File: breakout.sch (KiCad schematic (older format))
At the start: 36 parts, among them CON1 SD_Card, CON2 USB-MICRO-AB, P2 CONN_01X40, P3 CONN_01X40, P4 CONN_01X40, P5 A-DF-09-A/KG-T4S, Q1 SIA461DJ-T1-GE3, Q2 IRLML2402TRPBF, SW1 SW_PUSH

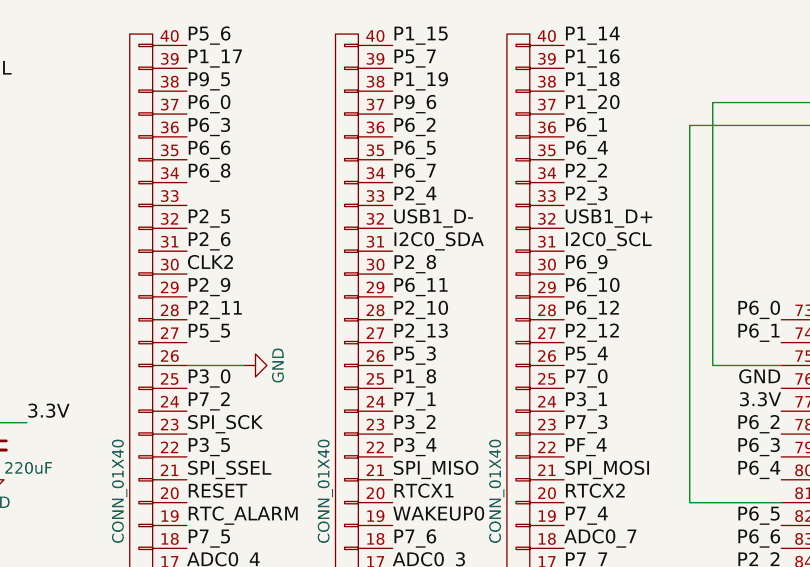
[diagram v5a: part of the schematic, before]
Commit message: P1_1 & P1_2 to header; trace move to aid GND plane
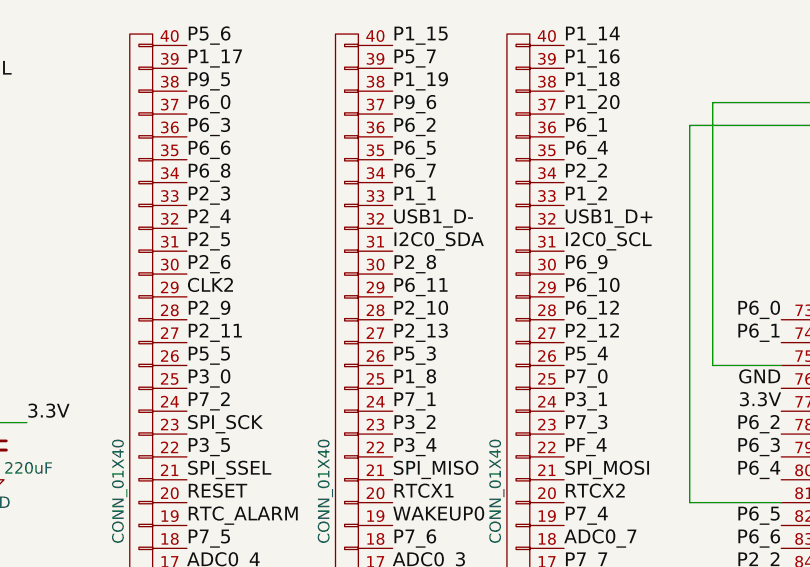
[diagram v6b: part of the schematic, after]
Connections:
- net CLK2: now also P2.29 (P29); no longer P2.30 (P30)
- net GND: no longer P2.26 (P26)
- net P1_1: now also P3.33 (P33)
- net P1_2: now also P4.33 (P33)
- net P2_11: now also P2.27 (P27); no longer P2.28 (P28)
- net P2_3: now also P2.33 (P33); no longer P4.33 (P33)
- net P2_4: now also P2.32 (P32); no longer P3.33 (P33)
- net P2_5: now also P2.31 (P31); no longer P2.32 (P32)
- net P2_6: now also P2.30 (P30); no longer P2.31 (P31)
- net P2_9: now also P2.28 (P28); no longer P2.29 (P29)
- net P5_5: now also P2.26 (P26); no longer P2.27 (P27)
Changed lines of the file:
@@
 Text Label 4500 1600 0    60   ~ 0
 I2C0_SCL
-Text Label 2850 1500 0    60   ~ 0
+Text Label 2850 1600 0    60   ~ 0
 P2_5
 Text Label 3750 1500 0    60   ~ 0
@@
 Text Label 4500 1500 0    60   ~ 0
 USB1_D+
-Text Label 3750 1400 0    60   ~ 0
+Text Label 2850 1500 0    60   ~ 0
 P2_4
 Text Label 2850 1300 0    60   ~ 0
@@
 Text Label 4500 2000 0    60   ~ 0
 P2_12
-Text Label 2850 1900 0    60   ~ 0
+Text Label 2850 2000 0    60   ~ 0
 P2_11
 Text Label 3750 1900 0    60   ~ 0
@@
 Text Label 4500 1900 0    60   ~ 0
 P6_12
-Text Label 2850 1800 0    60   ~ 0
+Text Label 2850 1900 0    60   ~ 0
 P2_9
 Text Label 3750 1800 0    60   ~ 0
@@
 Text Label 4500 1800 0    60   ~ 0
 P6_10
-Text Label 2850 1700 0    60   ~ 0
+Text Label 2850 1800 0    60   ~ 0
 CLK2
 Text Label 3750 1700 0    60   ~ 0
@@
 Text Label 4500 1700 0    60   ~ 0
 P6_9
-Text Label 2850 1600 0    60   ~ 0
+Text Label 2850 1700 0    60   ~ 0
 P2_6
-Text Label 4500 1400 0    60   ~ 0
+Text Label 2850 1400 0    60   ~ 0
 P2_3
-Text Label 2850 2000 0    60   ~ 0
+Text Label 2850 2100 0    60   ~ 0
 P5_5
 Text Label 4500 2100 0    60   ~ 0
@@
 	5050 2700 5450 2700
 $Comp
-L GND #PWR018
-U 1 1 566387B9
-P 3100 2100
-F 0 "#PWR018" H 3100 1850 50  0001 C CNN
-F 1 "GND" H 3100 1950 50  0000 C CNN
-F 2 "" H 3100 2100 60  0000 C CNN
-F 3 "" H 3100 2100 60  0000 C CNN
-	1    3100 2100
-	0    -1   -1   0
-$EndComp
-Wire Wire Line
-	2850 2100 3100 2100
-$Comp
 L SIA461DJ-T1-GE3 Q1
 U 1 1 5664957E
@@
 $EndComp
 $Comp
-L GND #PWR019
+L GND #PWR018
 U 1 1 56644987
 P 800 4900
-F 0 "#PWR019" H 800 4650 50  0001 C CNN
+F 0 "#PWR018" H 800 4650 50  0001 C CNN
 F 1 "GND" H 800 4750 50  0000 C CNN
 F 2 "" H 800 4900 60  0000 C CNN
@@
 3.3V
 $Comp
-L GND #PWR020
+L GND #PWR019
 U 1 1 566486A9
 P 7800 6800
-F 0 "#PWR020" H 7800 6550 50  0001 C CNN
+F 0 "#PWR019" H 7800 6550 50  0001 C CNN
 F 1 "GND" H 7800 6650 50  0000 C CNN
 F 2 "" H 7800 6800 60  0000 C CNN
@@
 	7800 6800 7450 6800
 $Comp
-L GND #PWR021
+L GND #PWR020
 U 1 1 5664879C
 P 7800 7150
-F 0 "#PWR021" H 7800 6900 50  0001 C CNN
+F 0 "#PWR020" H 7800 6900 50  0001 C CNN
 F 1 "GND" H 7800 7000 50  0000 C CNN
 F 2 "" H 7800 7150 60  0000 C CNN
@@
 Text Label 2850 2700 0    60   ~ 0
 RESET
+Text Label 4500 1400 0    60   ~ 0
+P1_2
+Text Label 3750 1400 0    60   ~ 0
+P1_1
 $EndSCHEMATC

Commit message: RAIL, UNREG, 5V
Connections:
- net 5V: now also P4.1 (P1)
- net GND: now also P2.1 (P1), P3.1 (P1), P4.2 (P2)
- net RAIL: now also P4.4 (P4)
- net UNREG: now reaches D2.1 (A), POWER1.2 (P2)
- net UNREG: now also P4.3 (P3)
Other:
- moved on the sheet: D2
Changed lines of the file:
@@
 Text Label 1600 750  0    60   ~ 0
 GND
-Text Label 1900 850  0    60   ~ 0
+Text Label 2050 850  0    60   ~ 0
 RAIL
 Text Label 5450 5500 2    60   ~ 0
@@
 L D_Schottky D2
 U 1 1 564CF908
-P 1750 850
-F 0 "D2" H 1850 800 50  0000 C CNN
-F 1 "B340" H 1700 950 50  0000 C CNN
-F 2 "Diodes_SMD:Diode-SMC_Standard" H 1750 850 60  0001 C CNN
-F 3 "" H 1750 850 60  0000 C CNN
-	1    1750 850
+P 1900 850
+F 0 "D2" H 2000 800 50  0000 C CNN
+F 1 "B340" H 1850 950 50  0000 C CNN
+F 2 "Diodes_SMD:Diode-SMC_Standard" H 1900 850 60  0001 C CNN
+F 3 "" H 1900 850 60  0000 C CNN
+	1    1900 850
 	1    0    0    1
 $EndComp
@@
 	900  6350 1000 6450
 Wire Bus Line
-	2600 6350 850  6350
+	850  6350 2600 6350
 Connection ~ 2350 5800
 Text Label 2850 2700 0    60   ~ 0
@@
 Text Label 3750 1400 0    60   ~ 0
 P1_1
+Text Label 4500 4600 0    60   ~ 0
+5V
+Text Label 4500 4300 0    60   ~ 0
+RAIL
+Text Label 1500 1150 2    60   ~ 0
+UNREG
+Wire Wire Line
+	1600 850  1600 1150
+Wire Wire Line
+	1750 850  1600 850
+Wire Wire Line
+	1600 1150 1500 1150
+Text Label 4500 4400 0    60   ~ 0
+UNREG
+Text Label 4500 4500 0    60   ~ 0
+GND
+Text Label 3750 4600 0    60   ~ 0
+GND
+Text Label 2850 4600 0    60   ~ 0
+GND
 $EndSCHEMATC

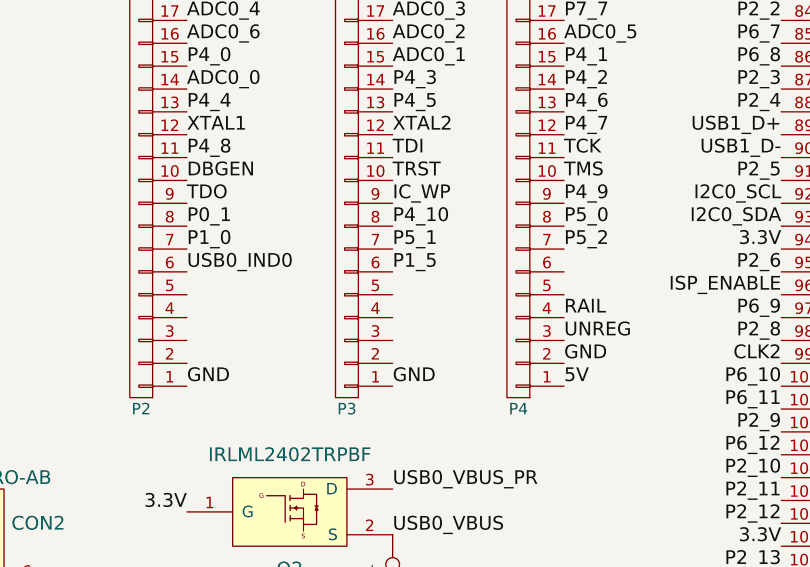
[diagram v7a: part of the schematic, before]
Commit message: added P1_3 and fixed annular ring of vias
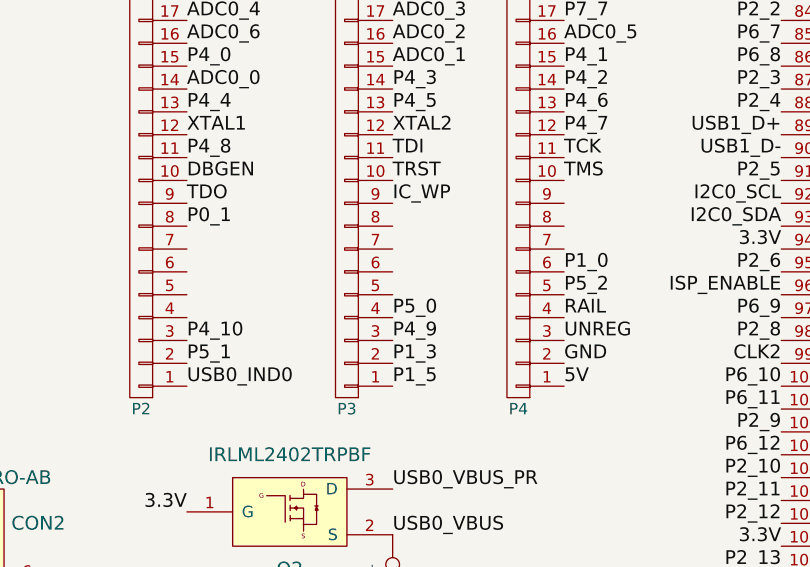
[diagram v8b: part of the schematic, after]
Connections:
- net GND: no longer P2.1 (P1), P3.1 (P1)
- net P1_0: now also P4.6 (P6); no longer P2.7 (P7)
- net P1_3: now also P3.2 (P2)
- net P1_5: now also P3.1 (P1); no longer P3.6 (P6)
- net P4_10: now also P2.3 (P3); no longer P3.8 (P8)
- net P4_9: now also P3.3 (P3); no longer P4.9 (P9)
- net P5_0: now also P3.4 (P4); no longer P4.8 (P8)
- net P5_1: now also P2.2 (P2); no longer P3.7 (P7)
- net P5_2: now also P4.5 (P5); no longer P4.7 (P7)
- net USB0_IND0: now also P2.1 (P1); no longer P2.6 (P6)
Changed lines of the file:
@@
 Text Label 2850 3800 0    60   ~ 0
 TDO
-Text Label 4500 3800 0    60   ~ 0
+Text Label 3750 4400 0    60   ~ 0
 P4_9
 Text Label 2850 3900 0    60   ~ 0
 P0_1
-Text Label 3750 3900 0    60   ~ 0
+Text Label 2850 4400 0    60   ~ 0
 P4_10
 Text Label 3750 3600 0    60   ~ 0
@@
 Text Label 3750 2200 0    60   ~ 0
 P1_8
-Text Label 3750 4100 0    60   ~ 0
+Text Label 3750 4600 0    60   ~ 0
 P1_5
-Text Label 2850 4100 0    60   ~ 0
+Text Label 2850 4600 0    60   ~ 0
 USB0_IND0
-Text Label 4500 4000 0    60   ~ 0
+Text Label 4500 4200 0    60   ~ 0
 P5_2
-Text Label 3750 4000 0    60   ~ 0
+Text Label 2850 4500 0    60   ~ 0
 P5_1
-Text Label 4500 3900 0    60   ~ 0
+Text Label 3750 4300 0    60   ~ 0
 P5_0
-Text Label 2850 4000 0    60   ~ 0
+Text Label 4500 4100 0    60   ~ 0
 P1_0
 $Comp
@@
 Text Label 4500 4500 0    60   ~ 0
 GND
-Text Label 3750 4600 0    60   ~ 0
-GND
-Text Label 2850 4600 0    60   ~ 0
-GND
+Text Label 3750 4500 0    60   ~ 0
+P1_3
 $EndSCHEMATC
